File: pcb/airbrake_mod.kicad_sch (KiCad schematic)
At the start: 3 parts

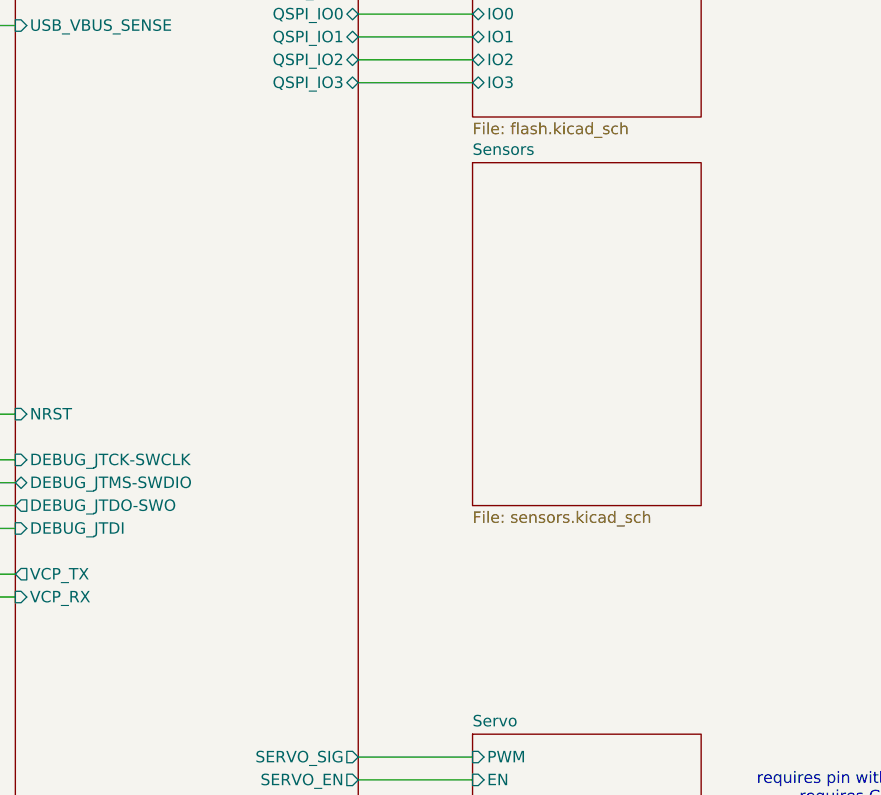
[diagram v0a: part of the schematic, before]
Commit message: Connected sensors SPI bus and signals to MCU
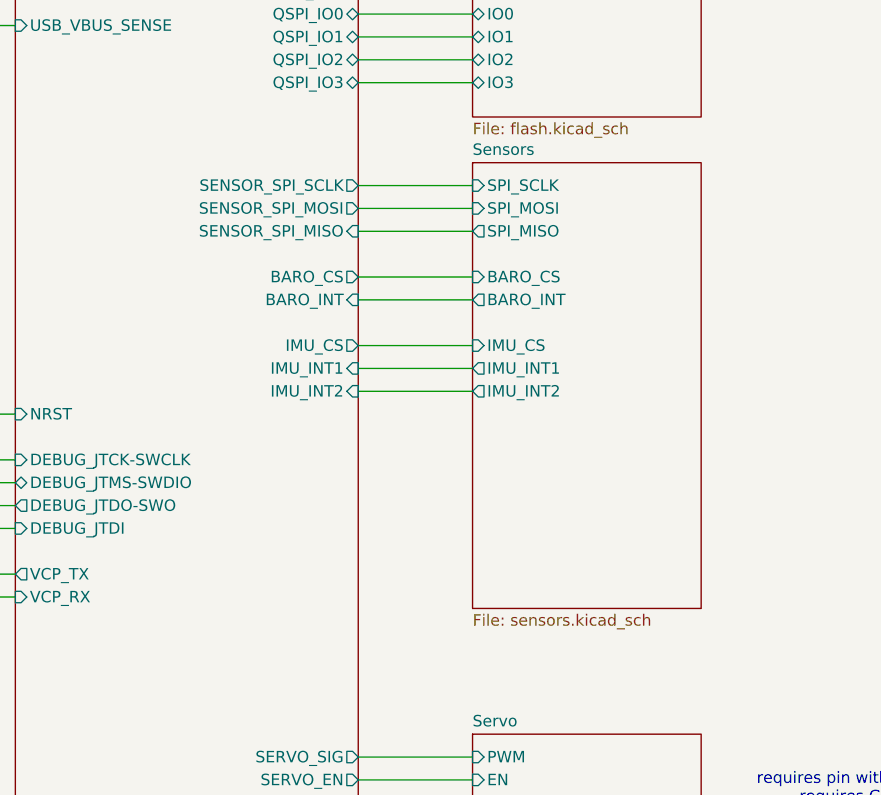
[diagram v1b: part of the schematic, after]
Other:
- sheet MCU ports: added BARO_CS, BARO_INT, IMU_CS, IMU_INT1, IMU_INT2, SENSOR_SPI_MISO, SENSOR_SPI_MOSI, SENSOR_SPI_SCLK; removed none
- sheet Sensors ports: added BARO_CS, BARO_INT, IMU_CS, IMU_INT1, IMU_INT2, SPI_MISO, SPI_MOSI, SPI_SCLK; removed none
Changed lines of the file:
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@@
+	(wire
+		(pts
+			(xy 101.6 71.12) (xy 114.3 71.12)
+		)
+		(stroke
+			(width 0)
+			(type default)
+		)
+	)
 	(wire
 		(pts
@@
 	(wire
 		(pts
+			(xy 101.6 53.34) (xy 114.3 53.34)
+		)
+		(stroke
+			(width 0)
+			(type default)
+		)
+	)
+	(wire
+		(pts
+			(xy 101.6 63.5) (xy 114.3 63.5)
+		)
+		(stroke
+			(width 0)
+			(type default)
+		)
+	)
+	(wire
+		(pts
 			(xy 101.6 119.38) (xy 114.3 119.38)
 		)
@@
 	(wire
 		(pts
+			(xy 101.6 76.2) (xy 114.3 76.2)
+		)
+		(stroke
+			(width 0)
+			(type default)
+		)
+	)
+	(wire
+		(pts
 			(xy 50.8 83.82) (xy 63.5 83.82)
 		)
@@
 	(wire
 		(pts
+			(xy 101.6 73.66) (xy 114.3 73.66)
+		)
+		(stroke
+			(width 0)
+			(type default)
+		)
+	)
+	(wire
+		(pts
 			(xy 101.6 39.37) (xy 114.3 39.37)
 		)
@@
 	(wire
 		(pts
+			(xy 101.6 55.88) (xy 114.3 55.88)
+		)
+		(stroke
+			(width 0)
+			(type default)
+		)
+	)
+	(wire
+		(pts
 			(xy 50.8 91.44) (xy 63.5 91.44)
 		)
@@
 		(pts
 			(xy 50.8 27.94) (xy 63.5 27.94)
+		)
+		(stroke
+			(width 0)
+			(type default)
+		)
+	)
+	(wire
+		(pts
+			(xy 101.6 66.04) (xy 114.3 66.04)
+		)
+		(stroke
+			(width 0)
+			(type default)
+		)
+	)
+	(wire
+		(pts
+			(xy 101.6 58.42) (xy 114.3 58.42)
 		)
 		(stroke
@@
 			)
 		)
+		(pin "SENSOR_SPI_SCLK" output
+			(at 101.6 53.34 0)
+			(effects
+				(font
+					(size 1.27 1.27)
+				)
+				(justify right)
+			)
+		)
+		(pin "SENSOR_SPI_MISO" input
+			(at 101.6 58.42 0)
+			(effects
+				(font
+					(size 1.27 1.27)
+				)
+				(justify right)
+			)
+		)
+		(pin "SENSOR_SPI_MOSI" output
+			(at 101.6 55.88 0)
+			(effects
+				(font
+					(size 1.27 1.27)
+				)
+				(justify right)
+			)
+		)
+		(pin "IMU_INT1" input
+			(at 101.6 73.66 0)
+			(effects
+				(font
+					(size 1.27 1.27)
+				)
+				(justify right)
+			)
+		)
+		(pin "IMU_INT2" input
+			(at 101.6 76.2 0)
+			(effects
+				(font
+					(size 1.27 1.27)
+				)
+				(justify right)
+			)
+		)
+		(pin "BARO_CS" output
+			(at 101.6 63.5 0)
+			(effects
+				(font
+					(size 1.27 1.27)
+				)
+				(justify right)
+			)
+		)
+		(pin "BARO_INT" input
+			(at 101.6 66.04 0)
+			(effects
+				(font
+					(size 1.27 1.27)
+				)
+				(justify right)
+			)
+		)
+		(pin "IMU_CS" output
+			(at 101.6 71.12 0)
+			(effects
+				(font
+					(size 1.27 1.27)
+				)
+				(justify right)
+			)
+		)
 		(instances
 			(project "airbrake_mod"
@@
 	(sheet
 		(at 114.3 50.8)
-		(size 25.4 38.1)
+		(size 25.4 49.53)
 		(exclude_from_sim no)
 		(in_bom yes)
@@
 		)
 		(property "Sheetfile" "sensors.kicad_sch"
-			(at 114.3 89.4846 0)
+			(at 114.3 100.9146 0)
 			(effects
 				(font
@@
 			)
 		)
+		(pin "IMU_CS" input
+			(at 114.3 71.12 180)
+			(effects
+				(font
+					(size 1.27 1.27)
+				)
+				(justify left)
+			)
+		)
+		(pin "IMU_INT1" output
+			(at 114.3 73.66 180)
+			(effects
+				(font
+					(size 1.27 1.27)
+				)
+				(justify left)
+			)
+		)
+		(pin "IMU_INT2" output
+			(at 114.3 76.2 180)
+			(effects
+				(font
+					(size 1.27 1.27)
+				)
+				(justify left)
+			)
+		)
+		(pin "SPI_SCLK" input
+			(at 114.3 53.34 180)
+			(effects
+				(font
+					(size 1.27 1.27)
+				)
+				(justify left)
+			)
+		)
+		(pin "SPI_MOSI" input
+			(at 114.3 55.88 180)
+			(effects
+				(font
+					(size 1.27 1.27)
+				)
+				(justify left)
+			)
+		)
+		(pin "SPI_MISO" output
+			(at 114.3 58.42 180)
+			(effects
+				(font
+					(size 1.27 1.27)
+				)
+				(justify left)
+			)
+		)
+		(pin "BARO_INT" output
+			(at 114.3 66.04 180)
+			(effects
+				(font
+					(size 1.27 1.27)
+				)
+				(justify left)
+			)
+		)
+		(pin "BARO_CS" input
+			(at 114.3 63.5 180)
+			(effects
+				(font
+					(size 1.27 1.27)
+				)
+				(justify left)
+			)
+		)

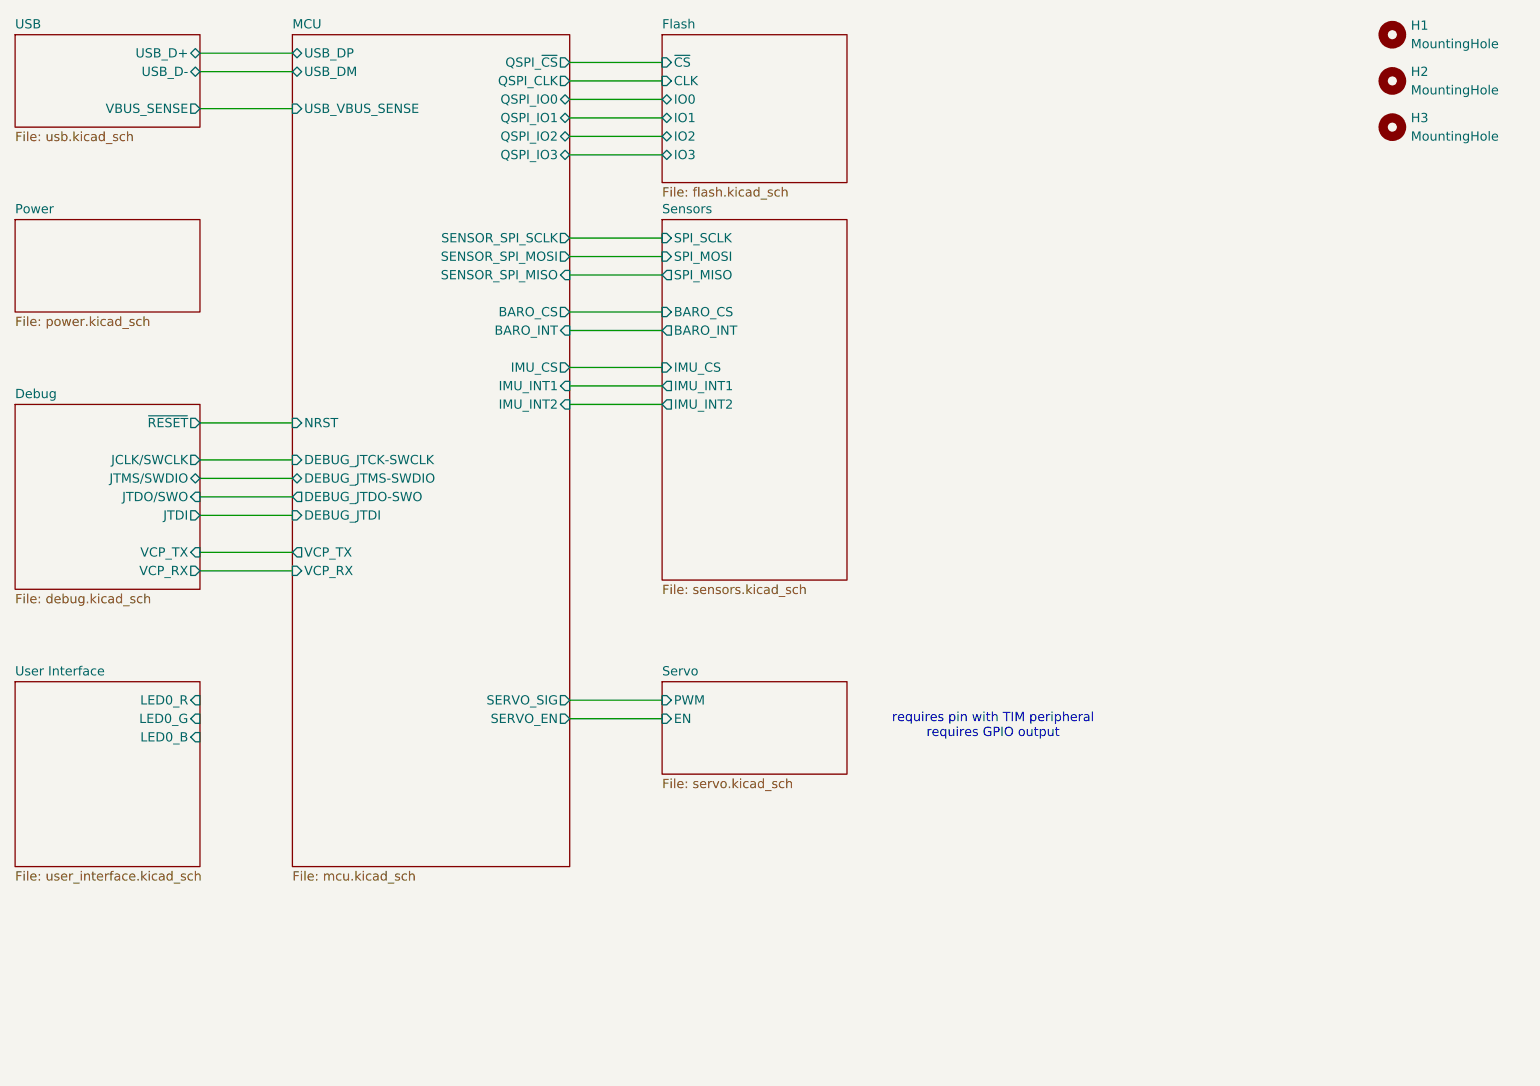
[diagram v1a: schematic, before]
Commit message: Add buzzer and move servo
Buzzer - TIM16 CH1 PB8
Servo - TIM17 CH1 PB9
SERVO_EN PE0
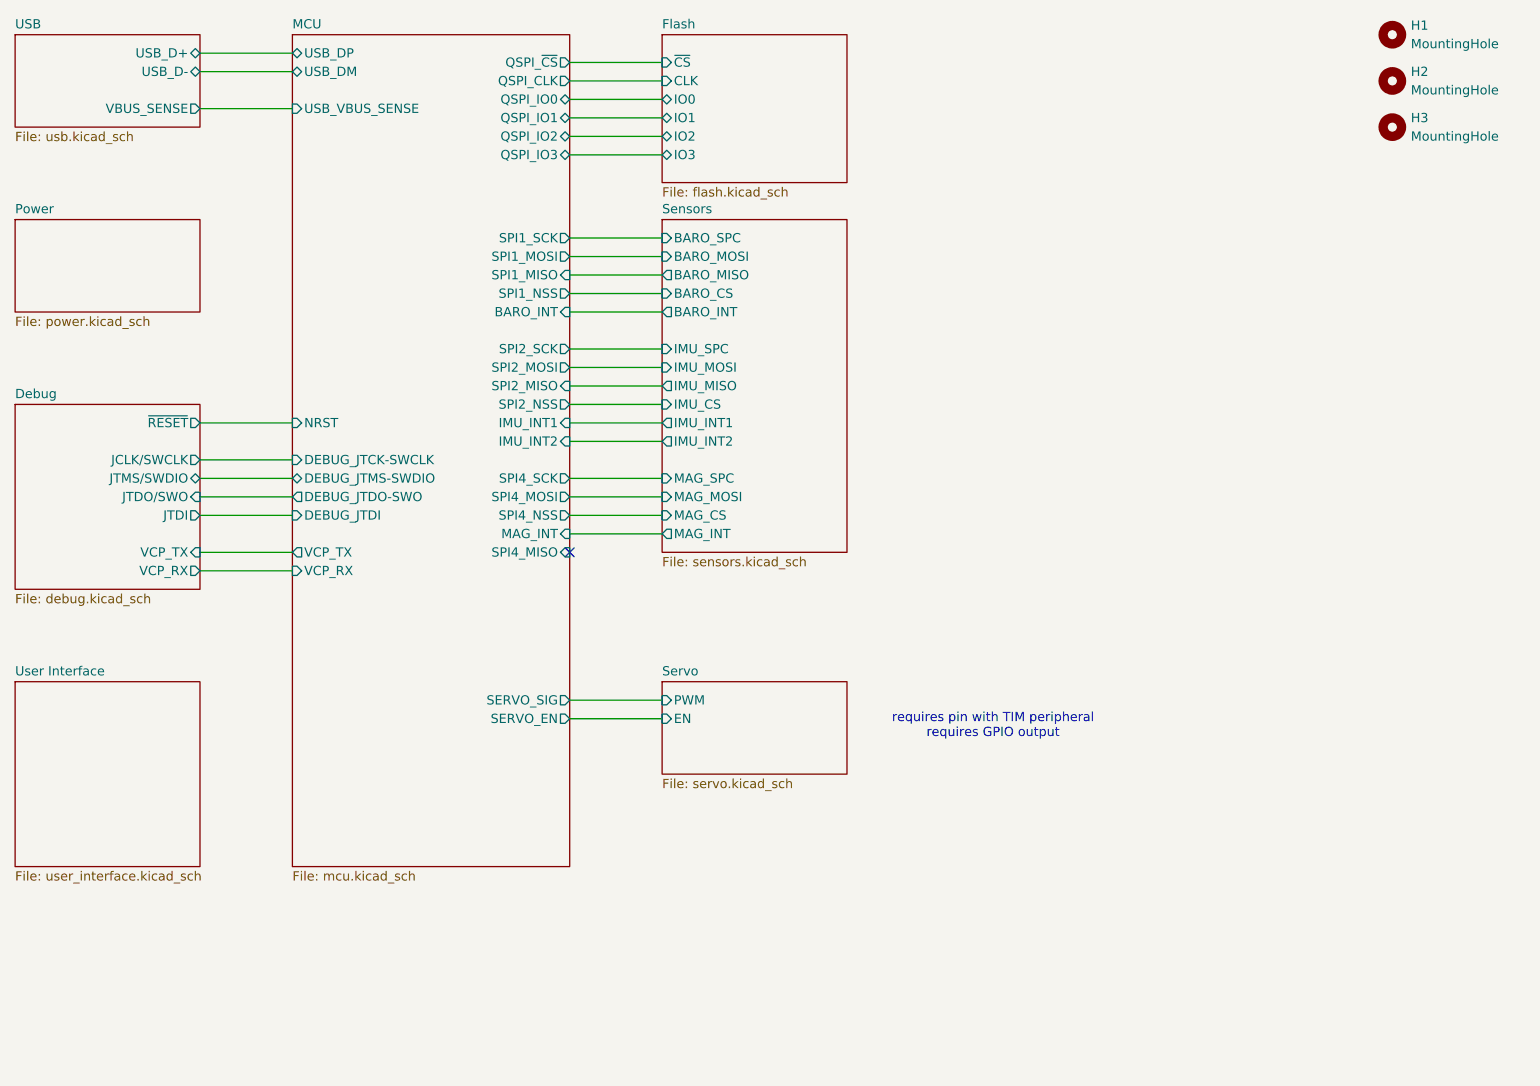
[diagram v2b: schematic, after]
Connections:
- no-connect marks 0 -> 1
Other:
- sheet MCU ports: added MAG_INT, SPI1_MISO, SPI1_MOSI, SPI1_NSS, SPI1_SCK, SPI2_MISO, SPI2_MOSI, SPI2_NSS, SPI2_SCK, SPI4_MISO, SPI4_MOSI, SPI4_NSS, SPI4_SCK; removed BARO_CS, IMU_CS, SENSOR_SPI_MISO, SENSOR_SPI_MOSI, SENSOR_SPI_SCLK
- sheet Sensors ports: added BARO_MISO, BARO_MOSI, BARO_SPC, IMU_MISO, IMU_MOSI, IMU_SPC, MAG_CS, MAG_INT, MAG_MOSI, MAG_SPC; removed SPI_MISO, SPI_MOSI, SPI_SCLK
- sheet User Interface ports: added none; removed LED0_B, LED0_G, LED0_R

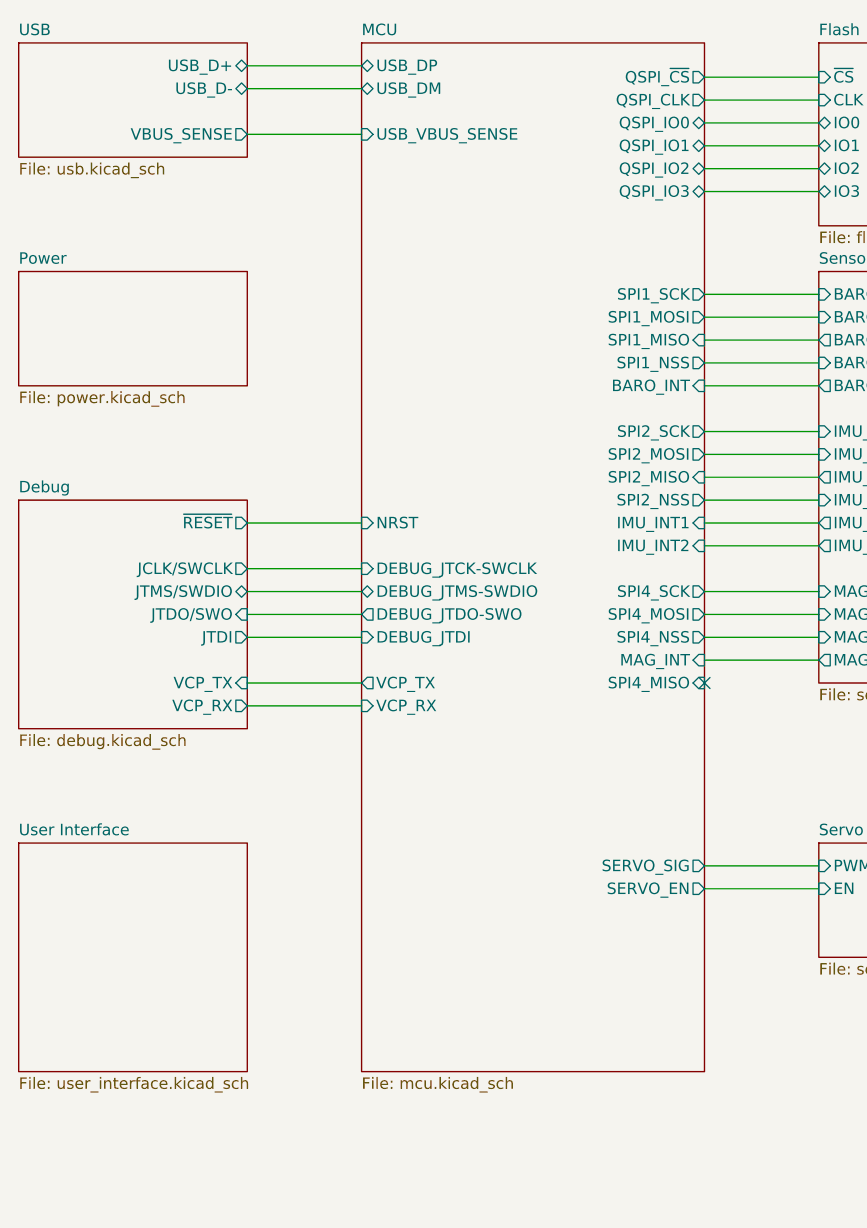
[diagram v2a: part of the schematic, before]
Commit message: Enable TIM3 and TIM4 for status LEDs
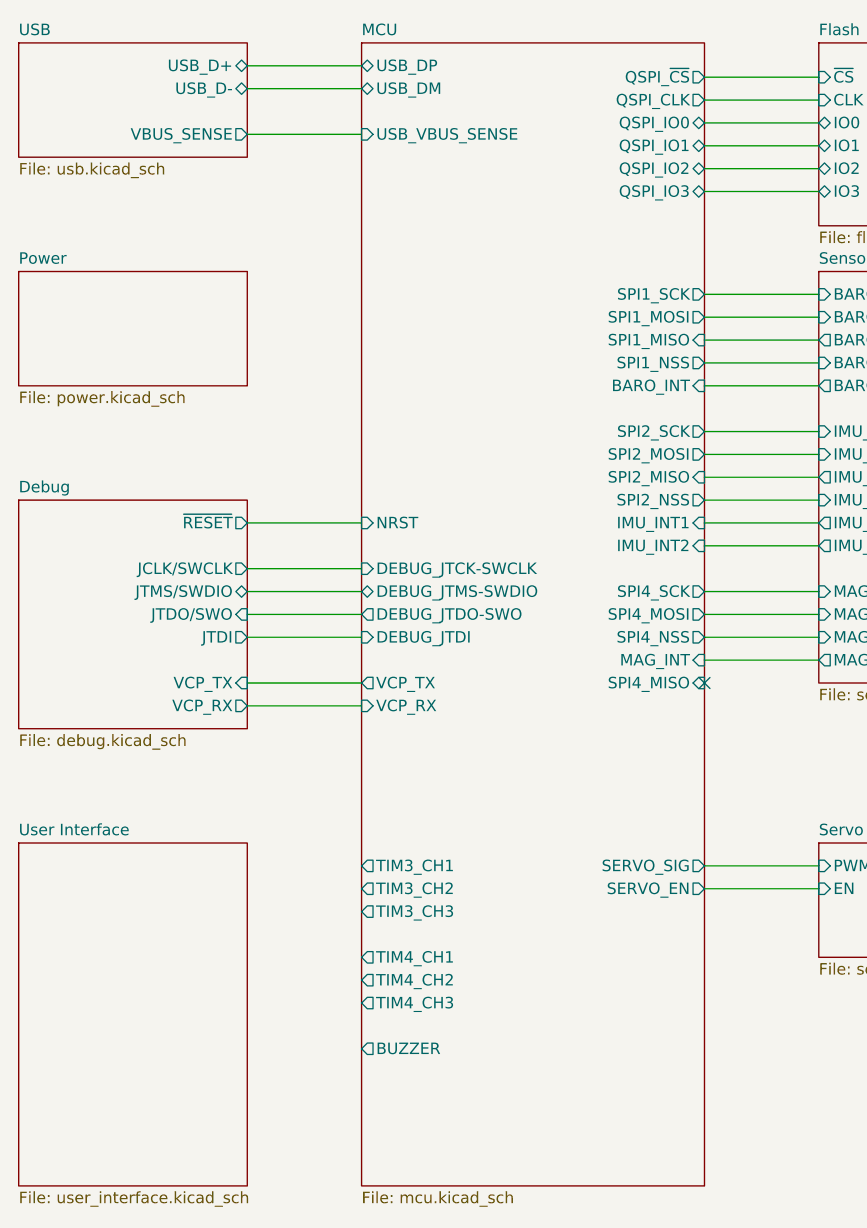
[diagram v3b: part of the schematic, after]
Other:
- sheet MCU ports: added BUZZER, TIM3_CH1, TIM3_CH2, TIM3_CH3, TIM4_CH1, TIM4_CH2, TIM4_CH3; removed none
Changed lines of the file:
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@@
 	(sheet
 		(at 25.4 114.3)
-		(size 25.4 25.4)
+		(size 25.4 38.1)
 		(exclude_from_sim no)
 		(in_bom yes)
@@
 		)
 		(property "Sheetfile" "user_interface.kicad_sch"
-			(at 25.4 140.2846 0)
+			(at 25.4 152.9846 0)
 			(effects
 				(font
@@
 	(sheet
 		(at 63.5 25.4)
-		(size 38.1 114.3)
+		(size 38.1 127)
 		(exclude_from_sim no)
 		(in_bom yes)
@@
 		)
 		(property "Sheetfile" "mcu.kicad_sch"
-			(at 63.5 140.2846 0)
+			(at 63.5 152.9846 0)
 			(effects
 				(font
@@
 			)
 		)
+		(pin "TIM3_CH3" output
+			(at 63.5 121.92 180)
+			(effects
+				(font
+					(size 1.27 1.27)
+				)
+				(justify left)
+			)
+		)
+		(pin "TIM3_CH1" output
+			(at 63.5 116.84 180)
+			(effects
+				(font
+					(size 1.27 1.27)
+				)
+				(justify left)
+			)
+		)
+		(pin "TIM3_CH2" output
+			(at 63.5 119.38 180)
+			(effects
+				(font
+					(size 1.27 1.27)
+				)
+				(justify left)
+			)
+		)
+		(pin "BUZZER" output
+			(at 63.5 137.16 180)
+			(effects
+				(font
+					(size 1.27 1.27)
+				)
+				(justify left)
+			)
+		)
+		(pin "TIM4_CH2" output
+			(at 63.5 129.54 180)
+			(effects
+				(font
+					(size 1.27 1.27)
+				)
+				(justify left)
+			)
+		)
+		(pin "TIM4_CH3" output
+			(at 63.5 132.08 180)
+			(effects
+				(font
+					(size 1.27 1.27)
+				)
+				(justify left)
+			)
+		)
+		(pin "TIM4_CH1" output
+			(at 63.5 127 180)
+			(effects
+				(font
+					(size 1.27 1.27)
+				)
+				(justify left)
+			)
+		)

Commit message: Finished user interface
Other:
- sheet MCU ports: added BATT_SENSE, BTN_0, BTN_1, BTN_2, BTN_3, MODE_1, MODE_2, MODE_4, MODE_C; removed none
- sheet Power ports: added BATT_SENSE; removed none
- sheet User Interface ports: added BTN_0, BTN_1, BTN_2, BTN_3, BUZZER, LED0_B, LED0_G, LED0_R, LED1_B, LED1_G, LED1_R, MODE_1, MODE_2, MODE_4, MODE_C; removed none
- note removed: "requires pin with TIM peripheral requires GPIO output"

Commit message: Start layout
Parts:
- H1, H2, H3: footprint (none) -> MountingHole:MountingHole_3.2mm_M3
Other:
- sheet MCU ports: added BATT_ISENSE, BATT_VSENSE, I2C1_SCL, I2C1_SDA; removed BATT_SENSE
- sheet Power ports: added BATT_ISENSE, BATT_VSENSE; removed BATT_SENSE
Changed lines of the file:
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@@
+	(wire
+		(pts
+			(xy 50.8 55.88) (xy 63.5 55.88)
+		)
+		(stroke
+			(width 0)
+			(type default)
+		)
+	)
 	(wire
 		(pts
@@
 			)
 		)
-		(property "Footprint" ""
+		(property "Footprint" "MountingHole:MountingHole_3.2mm_M3"
 			(at 214.63 25.4 0)
 			(effects
@@
 			)
 		)
-		(property "Footprint" ""
+		(property "Footprint" "MountingHole:MountingHole_3.2mm_M3"
 			(at 214.63 38.1 0)
 			(effects
@@
 			)
 		)
-		(property "Footprint" ""
+		(property "Footprint" "MountingHole:MountingHole_3.2mm_M3"
 			(at 214.63 31.75 0)
 			(effects
@@
 			)
 		)
-		(pin "BATT_SENSE" input
+		(pin "BATT_VSENSE" input
 			(at 63.5 53.34 180)
 			(effects
@@
 				)
 				(justify left)
+			)
+		)
+		(pin "BATT_ISENSE" input
+			(at 63.5 55.88 180)
+			(effects
+				(font
+					(size 1.27 1.27)
+				)
+				(justify left)
+			)
+		)
+		(pin "I2C1_SDA" bidirectional
+			(at 101.6 142.24 0)
+			(effects
+				(font
+					(size 1.27 1.27)
+				)
+				(justify right)
+			)
+		)
+		(pin "I2C1_SCL" output
+			(at 101.6 144.78 0)
+			(effects
+				(font
+					(size 1.27 1.27)
+				)
+				(justify right)
 			)
 		)
@@
 			)
 		)
-		(pin "BATT_SENSE" output
+		(pin "BATT_VSENSE" output
 			(at 50.8 53.34 0)
 			(effects
 				(font
+					(size 1.27 1.27)
+				)
+				(justify right)
+			)
+		)
+		(pin "BATT_ISENSE" output
+			(at 50.8 55.88 0)
+			(effects
+				(font

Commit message: Layout power
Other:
- sheet MCU ports: added USB_D+, USB_D-; removed USB_DM, USB_DP
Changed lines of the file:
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@@
-			)
-		)
-		(pin "USB_DP" bidirectional
-			(at 63.5 27.94 180)
-			(effects
-				(font
-					(size 1.27 1.27)
-				)
-				(justify left)
-			)
-		)
-		(pin "USB_DM" bidirectional
-			(at 63.5 30.48 180)
-			(effects
-				(font
-					(size 1.27 1.27)
-				)
-				(justify left)
 			)
 		)
@@
 			)
 		)
+		(pin "USB_D-" bidirectional
+			(at 63.5 30.48 180)
+			(effects
+				(font
+					(size 1.27 1.27)
+				)
+				(justify left)
+			)
+		)
+		(pin "USB_D+" bidirectional
+			(at 63.5 27.94 180)
+			(effects
+				(font
+					(size 1.27 1.27)
+				)
+				(justify left)
+			)
+		)
